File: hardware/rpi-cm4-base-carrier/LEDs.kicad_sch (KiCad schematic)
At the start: 17 parts, among them IC2 KTD2052BEVAA-TR, U2 74LVC1G07SE-7

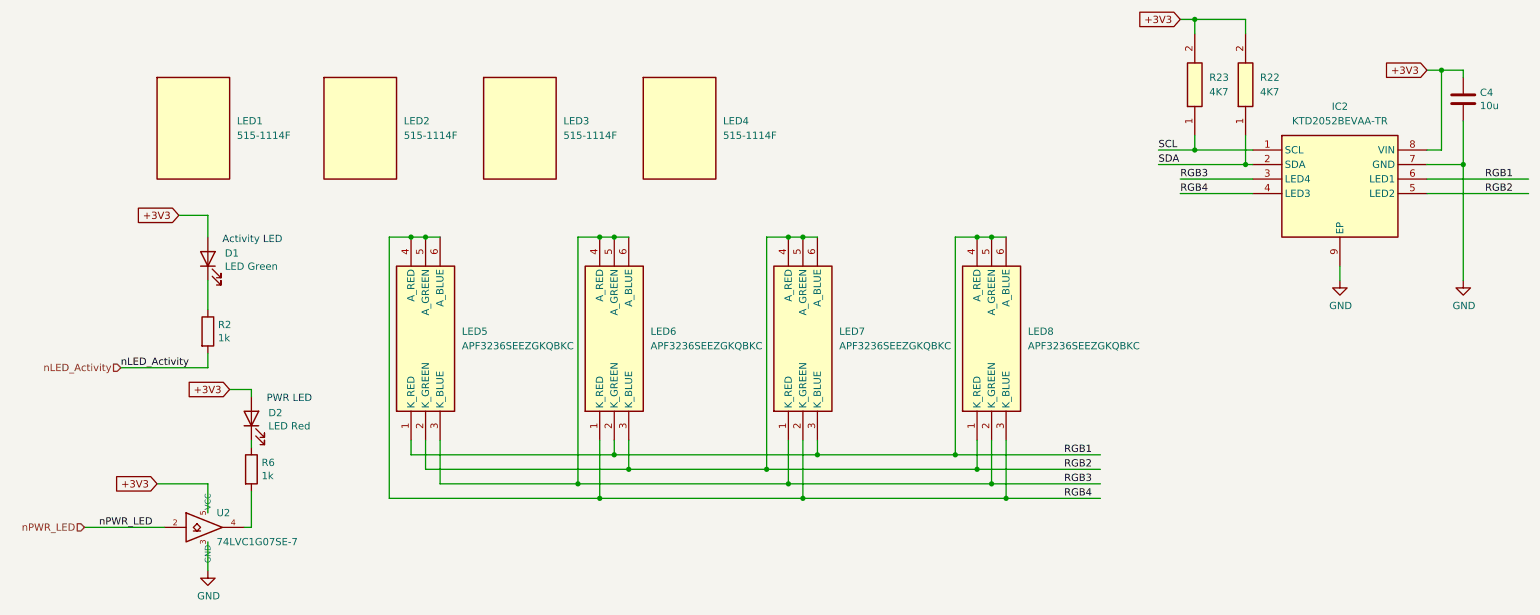
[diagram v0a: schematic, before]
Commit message: started final placement of blocks, realised ESD suppression devices cannot be manufactured with JLC, need to switch part
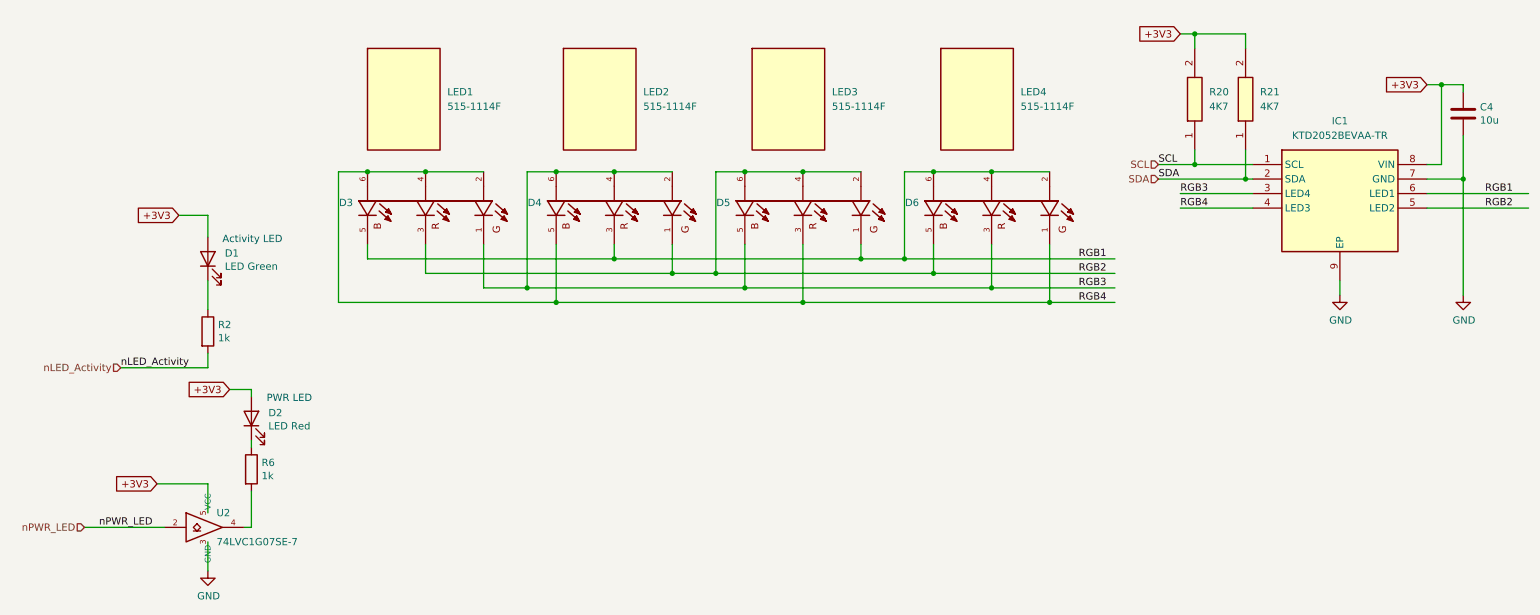
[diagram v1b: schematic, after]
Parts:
- removed LED5, LED6, LED7, LED8: APF3236SEEZGKQBKC, APF3236SEEZGKQBKC, symbol SamacSys_Parts:APF3236SEEZGKQBKC
- added D3, D4, D5, D6: 19-337C_RSBHGHC-A88_4T, 19_337C_RSBHGHC_A88_4T:LED_19-337C_RSBHGHC-A88_4T, symbol 19-337C_RSBHGHC-A88_4T:19-337C_RSBHGHC-A88_4T
- IC1: renamed from IC2; footprint SON50P200X200X58-9N -> SamacSys_Parts:SON50P200X200X58-9N
- LED1, LED2, LED3, LED4: footprint 515-1114F -> SamacSys_Parts:515-1114F
- R20: renamed from R23; footprint RESC1005X37N -> SamacSys_Parts:RESC1005X37N
- R21: renamed from R22; footprint RESC1005X37N -> SamacSys_Parts:RESC1005X37N
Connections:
- net RGB1: now also D3.5, D4.3, D5.1, D6.2, D6.4, D6.6
- net RGB2: now also D3.3, D4.1, D5.2, D5.4, D5.6, D6.5
- net RGB3: now also D3.1, D4.2, D4.4, D4.6, D5.5, D6.3
- net RGB4: now also D3.2, D3.4, D3.6, D4.5, D5.3, D6.1
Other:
- moved on the sheet: C4, IC1, LED1, LED2, LED3, LED4, R20, R21

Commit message: fan control added to sch, layout 90% complete, awaiting review
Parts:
- IC1: footprint SamacSys_Parts:SON50P200X200X58-9N -> SON50P200X200X58-9N
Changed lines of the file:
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@@
       (effects (font (size 1.27 1.27)))
     )
-    (property "Footprint" "SamacSys_Parts:SON50P200X200X58-9N" (at 256.54 134.29 0)
+    (property "Footprint" "SON50P200X200X58-9N" (at 256.54 134.29 0)
       (effects (font (size 1.27 1.27)) (justify left top) hide)
     )

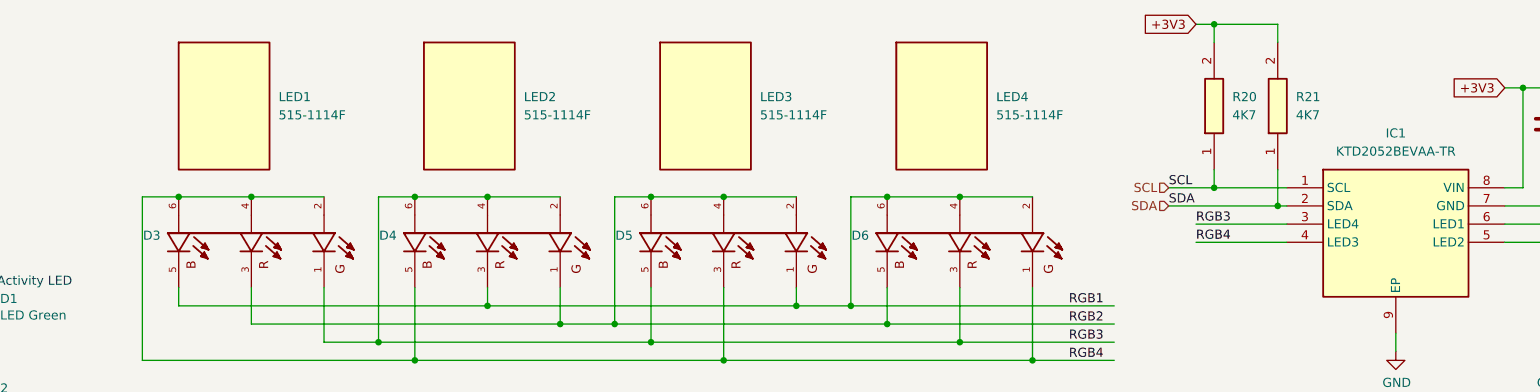
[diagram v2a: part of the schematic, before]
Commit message: convert IC refs to U refs and re-annotate, add fiducials and extra via stitching to layout
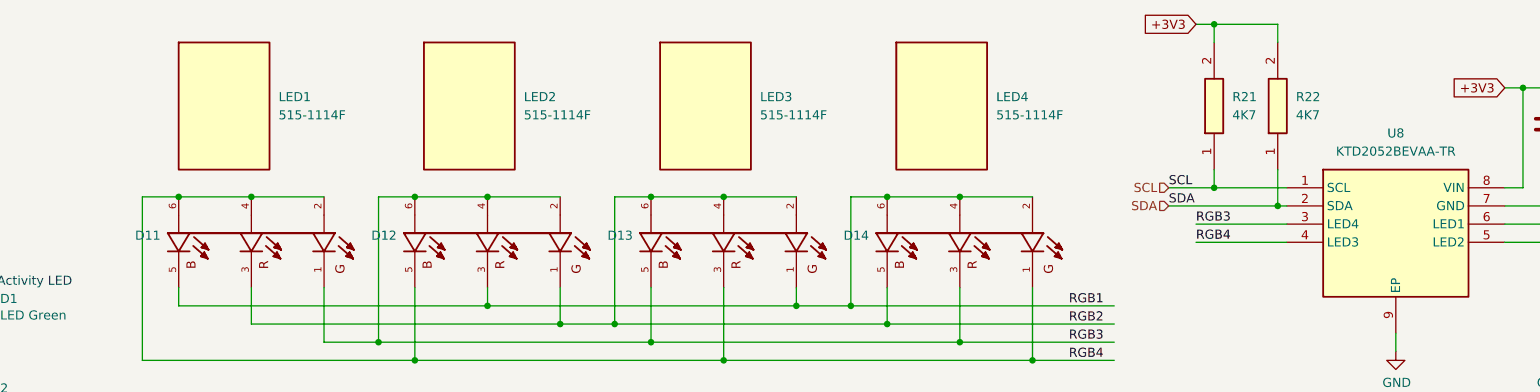
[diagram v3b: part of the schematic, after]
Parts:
- renumbered D3 to D11, D4 to D12, D5 to D13, D6 to D14, R20 to R21, R21 to R22, IC1 to U8
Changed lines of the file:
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@@
         )
         (path "/92c58705-ecb0-498b-b561-44a3f0daad57/fc4c71a5-1008-4ac4-98db-57c838c57d91/91188afb-aa0e-4641-b6d1-5b7addeddc93"
-          (reference "R18") (unit 1)
+          (reference "R19") (unit 1)
         )
       )
@@
         )
         (path "/92c58705-ecb0-498b-b561-44a3f0daad57/fc4c71a5-1008-4ac4-98db-57c838c57d91/91188afb-aa0e-4641-b6d1-5b7addeddc93"
-          (reference "#PWR050") (unit 1)
+          (reference "#PWR062") (unit 1)
         )
       )
@@
         )
         (path "/92c58705-ecb0-498b-b561-44a3f0daad57/fc4c71a5-1008-4ac4-98db-57c838c57d91/91188afb-aa0e-4641-b6d1-5b7addeddc93"
-          (reference "D1") (unit 1)
+          (reference "D9") (unit 1)
         )
       )
@@
         )
         (path "/92c58705-ecb0-498b-b561-44a3f0daad57/fc4c71a5-1008-4ac4-98db-57c838c57d91/91188afb-aa0e-4641-b6d1-5b7addeddc93"
-          (reference "#PWR051") (unit 1)
+          (reference "#PWR063") (unit 1)
         )
       )
@@
   (symbol (lib_id "19-337C_RSBHGHC-A88_4T:19-337C_RSBHGHC-A88_4T") (at 118.11 48.26 270) (unit 1)
     (in_bom yes) (on_board yes) (dnp no) (fields_autoplaced)
-    (property "Reference" "D4" (at 105.41 46.0471 90)
+    (property "Reference" "D12" (at 105.41 46.0471 90)
       (effects (font (size 1.27 1.27)) (justify right))
     )
@@
       (project "rpi-cm4-base-carrier"
         (path "/92c58705-ecb0-498b-b561-44a3f0daad57/fc4c71a5-1008-4ac4-98db-57c838c57d91/91188afb-aa0e-4641-b6d1-5b7addeddc93"
-          (reference "D4") (unit 1)
+          (reference "D12") (unit 1)
         )
       )
@@
         )
         (path "/92c58705-ecb0-498b-b561-44a3f0daad57/fc4c71a5-1008-4ac4-98db-57c838c57d91/91188afb-aa0e-4641-b6d1-5b7addeddc93"
-          (reference "C21") (unit 1)
+          (reference "C32") (unit 1)
         )
       )
@@
         )
         (path "/92c58705-ecb0-498b-b561-44a3f0daad57/fc4c71a5-1008-4ac4-98db-57c838c57d91/91188afb-aa0e-4641-b6d1-5b7addeddc93"
-          (reference "D2") (unit 1)
+          (reference "D10") (unit 1)
         )
       )
@@
         )
         (path "/92c58705-ecb0-498b-b561-44a3f0daad57/fc4c71a5-1008-4ac4-98db-57c838c57d91/91188afb-aa0e-4641-b6d1-5b7addeddc93"
-          (reference "#PWR049") (unit 1)
+          (reference "#PWR061") (unit 1)
         )
       )
@@
   (symbol (lib_id "19-337C_RSBHGHC-A88_4T:19-337C_RSBHGHC-A88_4T") (at 85.09 48.26 270) (unit 1)
     (in_bom yes) (on_board yes) (dnp no) (fields_autoplaced)
-    (property "Reference" "D3" (at 72.39 46.0471 90)
+    (property "Reference" "D11" (at 72.39 46.0471 90)
       (effects (font (size 1.27 1.27)) (justify right))
     )
@@
       (project "rpi-cm4-base-carrier"
         (path "/92c58705-ecb0-498b-b561-44a3f0daad57/fc4c71a5-1008-4ac4-98db-57c838c57d91/91188afb-aa0e-4641-b6d1-5b7addeddc93"
-          (reference "D3") (unit 1)
+          (reference "D11") (unit 1)
         )
       )
@@
   (symbol (lib_id "19-337C_RSBHGHC-A88_4T:19-337C_RSBHGHC-A88_4T") (at 151.13 48.26 270) (unit 1)
     (in_bom yes) (on_board yes) (dnp no) (fields_autoplaced)
-    (property "Reference" "D5" (at 138.43 46.0471 90)
+    (property "Reference" "D13" (at 138.43 46.0471 90)
       (effects (font (size 1.27 1.27)) (justify right))
     )
@@
       (project "rpi-cm4-base-carrier"
         (path "/92c58705-ecb0-498b-b561-44a3f0daad57/fc4c71a5-1008-4ac4-98db-57c838c57d91/91188afb-aa0e-4641-b6d1-5b7addeddc93"
-          (reference "D5") (unit 1)
+          (reference "D13") (unit 1)
         )
       )
@@
   (symbol (lib_id "SamacSys_Parts:MCS04020C4701FE000") (at 228.6 36.83 90) (unit 1)
     (in_bom yes) (on_board yes) (dnp no) (fields_autoplaced)
-    (property "Reference" "R21" (at 231.14 26.67 90)
+    (property "Reference" "R22" (at 231.14 26.67 90)
       (effects (font (size 1.27 1.27)) (justify right))
     )
@@
       (project "rpi-cm4-base-carrier"
         (path "/92c58705-ecb0-498b-b561-44a3f0daad57/fc4c71a5-1008-4ac4-98db-57c838c57d91/91188afb-aa0e-4641-b6d1-5b7addeddc93"
-          (reference "R21") (unit 1)
+          (reference "R22") (unit 1)
         )
       )
@@
   (symbol (lib_id "SamacSys_Parts:KTD2052BEVAA-TR") (at 229.87 39.37 0) (unit 1)
     (in_bom yes) (on_board yes) (dnp no) (fields_autoplaced)
-    (property "Reference" "IC1" (at 245.11 31.75 0)
+    (property "Reference" "U8" (at 245.11 31.75 0)
       (effects (font (size 1.27 1.27)))
     )
@@
       (project "rpi-cm4-base-carrier"
         (path "/92c58705-ecb0-498b-b561-44a3f0daad57/fc4c71a5-1008-4ac4-98db-57c838c57d91/91188afb-aa0e-4641-b6d1-5b7addeddc93"
-          (reference "IC1") (unit 1)
+          (reference "U8") (unit 1)
         )
       )
@@
         )
         (path "/92c58705-ecb0-498b-b561-44a3f0daad57/fc4c71a5-1008-4ac4-98db-57c838c57d91/91188afb-aa0e-4641-b6d1-5b7addeddc93"
-          (reference "R19") (unit 1)
+          (reference "R20") (unit 1)
         )
       )
@@
   (symbol (lib_id "SamacSys_Parts:MCS04020C4701FE000") (at 219.71 36.83 90) (unit 1)
     (in_bom yes) (on_board yes) (dnp no) (fields_autoplaced)
-    (property "Reference" "R20" (at 222.25 26.67 90)
+    (property "Reference" "R21" (at 222.25 26.67 90)
       (effects (font (size 1.27 1.27)) (justify right))
     )
@@
       (project "rpi-cm4-base-carrier"
         (path "/92c58705-ecb0-498b-b561-44a3f0daad57/fc4c71a5-1008-4ac4-98db-57c838c57d91/91188afb-aa0e-4641-b6d1-5b7addeddc93"
-          (reference "R20") (unit 1)
+          (reference "R21") (unit 1)
         )
       )
@@
   (symbol (lib_id "19-337C_RSBHGHC-A88_4T:19-337C_RSBHGHC-A88_4T") (at 184.15 48.26 270) (unit 1)
     (in_bom yes) (on_board yes) (dnp no) (fields_autoplaced)
-    (property "Reference" "D6" (at 171.45 46.0471 90)
+    (property "Reference" "D14" (at 171.45 46.0471 90)
       (effects (font (size 1.27 1.27)) (justify right))
     )
@@
       (project "rpi-cm4-base-carrier"
         (path "/92c58705-ecb0-498b-b561-44a3f0daad57/fc4c71a5-1008-4ac4-98db-57c838c57d91/91188afb-aa0e-4641-b6d1-5b7addeddc93"
-          (reference "D6") (unit 1)
+          (reference "D14") (unit 1)
         )
       )
@@
         )
         (path "/92c58705-ecb0-498b-b561-44a3f0daad57/fc4c71a5-1008-4ac4-98db-57c838c57d91/91188afb-aa0e-4641-b6d1-5b7addeddc93"
-          (reference "U9") (unit 1)
-        )
-      )
+          (reference "U7") (unit 1)
+        )
+      )

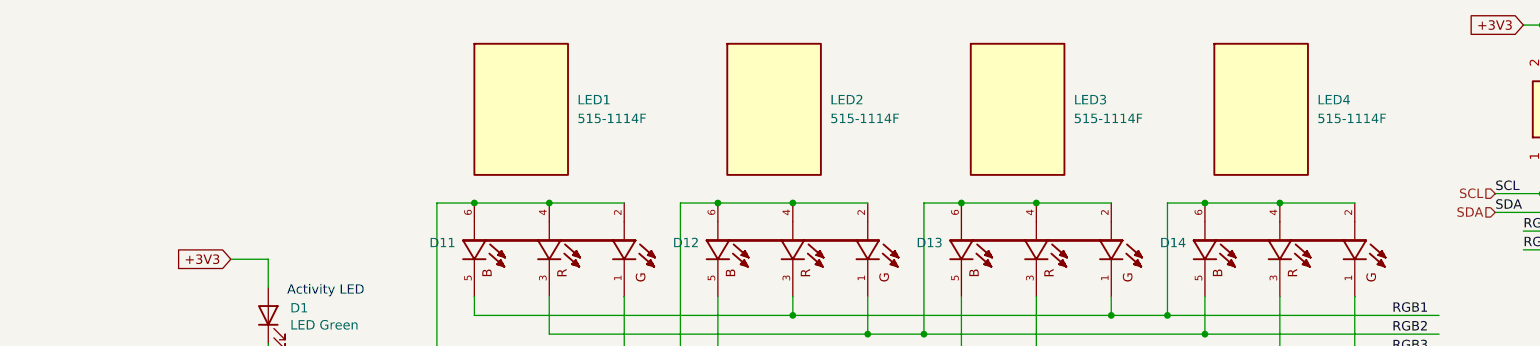
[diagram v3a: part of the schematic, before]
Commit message: design files exported ready for manufacture, LCSC part numbers added throughout the library
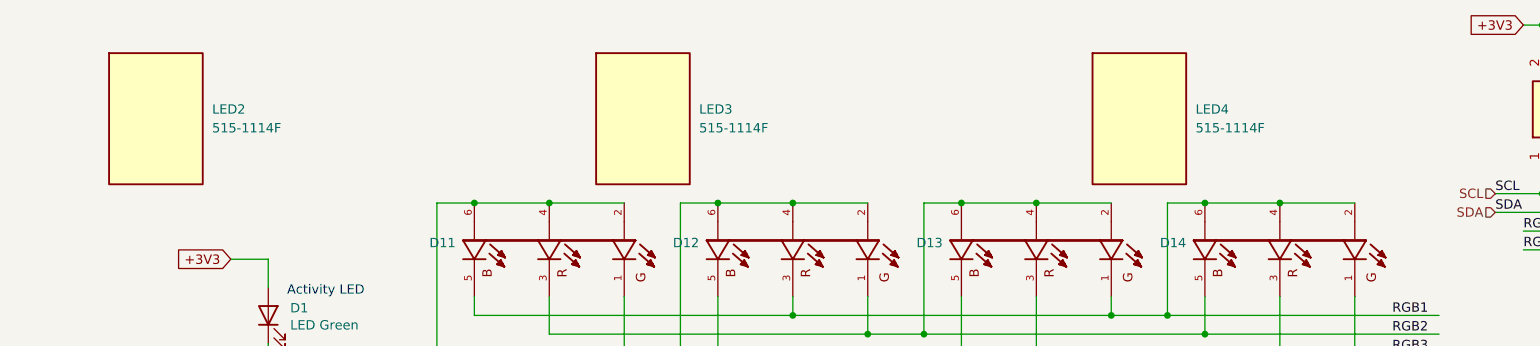
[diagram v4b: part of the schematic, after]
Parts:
- removed LED1: 515-1114F, SamacSys_Parts:515-1114F, symbol SamacSys_Parts:515-1114F
- C4: LCSC Part # (none) -> C326595; LCSC Part Number (none) -> C326595
- D1: LCSC Part # (none) -> C5879397; LCSC Part Number (none) -> C5879397
- D11, D12, D13, D14: LCSC Part # (none) -> C5274136; LCSC Part Number (none) -> C5274136
- D2: LCSC Part # (none) -> C5878870; LCSC Part Number (none) -> C5878870
- LED2, LED3, LED4: LCSC Part # (none) -> NF; LCSC Part Number (none) -> NF
- R2, R6: LCSC Part # (none) -> C131360; LCSC Part Number (none) -> C131360
- R21, R22: LCSC Part # (none) -> C159984; LCSC Part Number (none) -> C159984
- U2: LCSC Part # (none) -> C2675596; LCSC Part Number (none) -> C2675596
- U8: LCSC Part # (none) -> Non Stock; LCSC Part Number (none) -> Non Stock
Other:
- title: (none) -> Raspberry Pi Compute Module 4 Control Node
- moved on the sheet: LED2, LED3, LED4
